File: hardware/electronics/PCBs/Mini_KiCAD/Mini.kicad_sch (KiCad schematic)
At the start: 0 parts

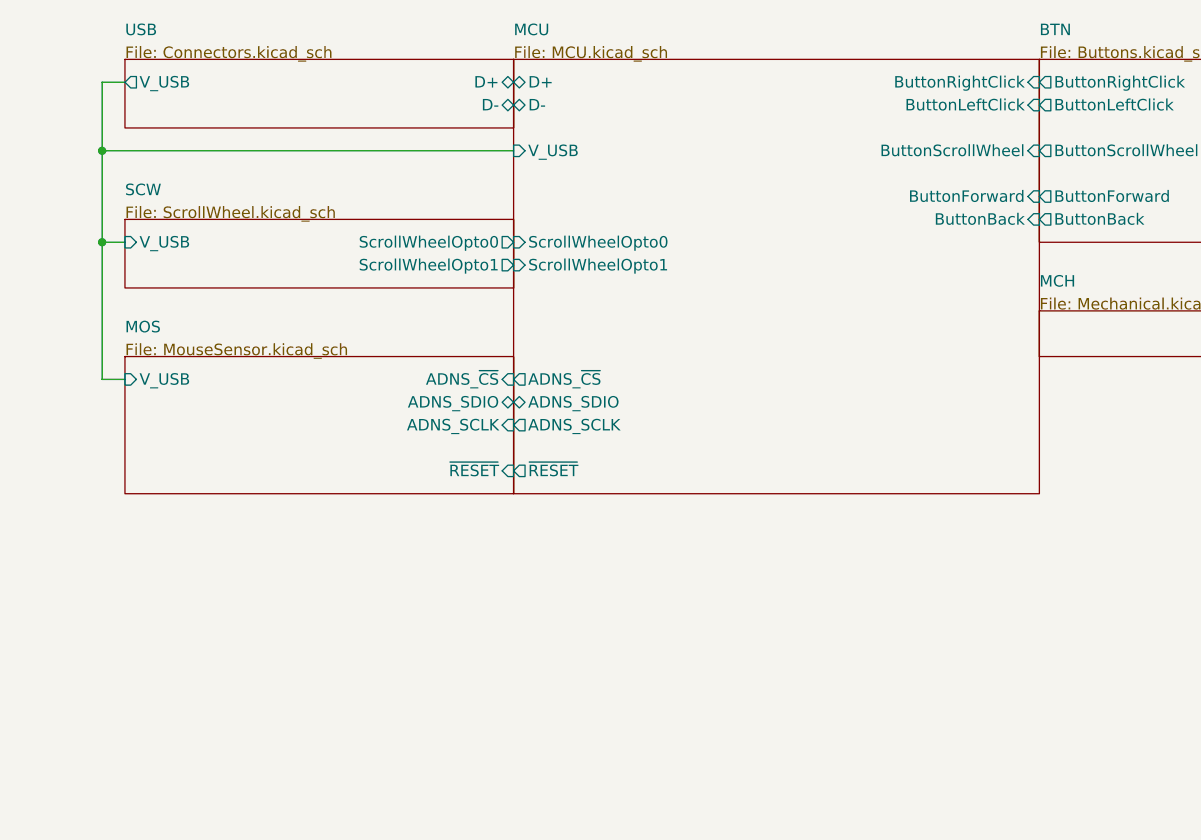
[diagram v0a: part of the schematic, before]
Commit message: Initial commit of the PCB project file replacing the ADNS-5050 with PMW3360, referencing the schematic of the Ploopy Classic.
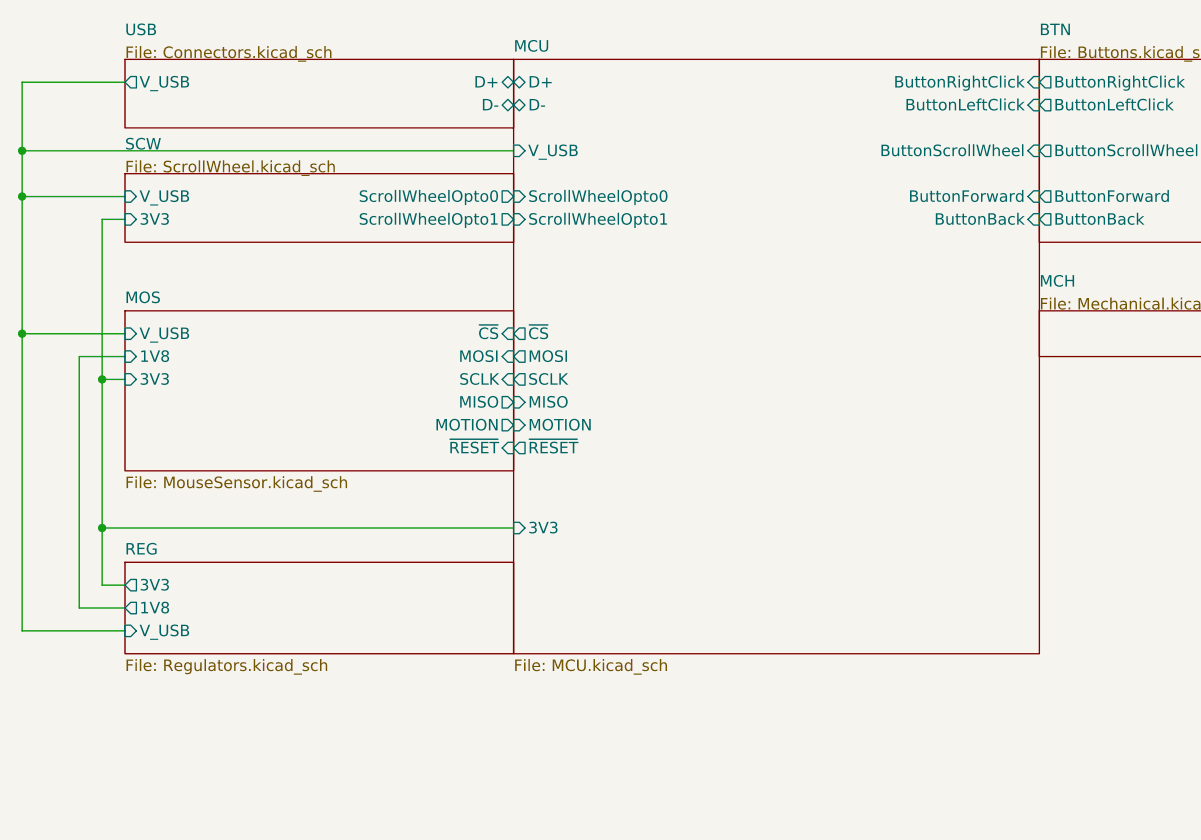
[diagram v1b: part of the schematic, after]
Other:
- added sheet REG (Regulators.kicad_sch)
- sheet MCU ports: added 3V3, MISO, MOSI, MOTION, SCLK, ~{CS}; removed ADNS_SCLK, ADNS_SDIO, ADNS_~{CS}
- sheet MOS ports: added 1V8, 3V3, MISO, MOSI, MOTION, SCLK, ~{CS}; removed ADNS_SCLK, ADNS_SDIO, ADNS_~{CS}
- sheet SCW ports: added 3V3; removed none
